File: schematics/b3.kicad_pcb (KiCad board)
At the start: 2 copper layers, 69.5 x 25 mm, 40 parts, among them J1 PowerInput, J2 PowerPassThru, J3 OutputPins, U1 INA128, U2 INA128, U3 INA128, U4 INA128

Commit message: polished b3 some more
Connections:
- J3 pad 2: /out3 -> /out2
- J3 pad 3: /out4 -> /out3
- J3 pad 4: /out2 -> /out4
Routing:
- net /out3: track 27.0 -> 31.2 mm
- net /out2: track 25.4 -> 28.0 mm, vias 0 -> 1
- net VCC: vias 7 -> 6
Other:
- board text added: "GND V+ Vref"
- board text added: "gain"
- board text added: "out1"
- board text added: "out4"

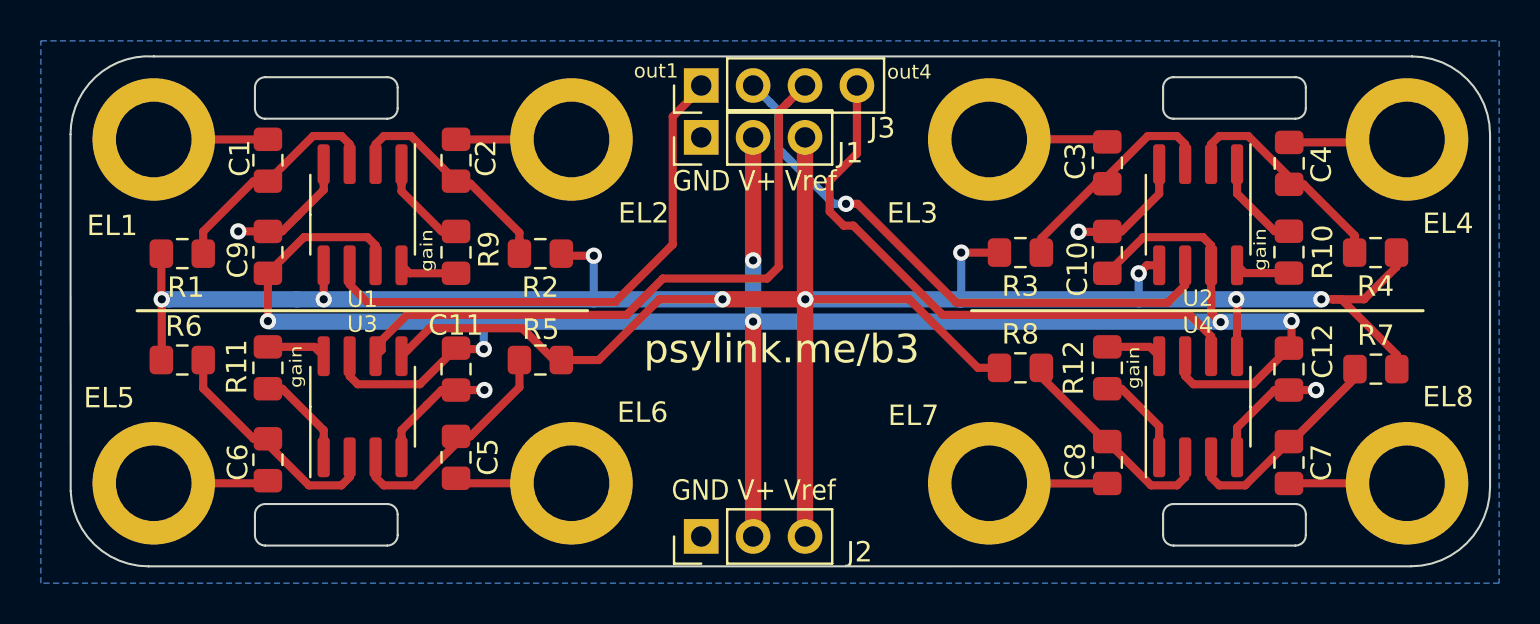
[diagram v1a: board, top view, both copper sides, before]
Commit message: enlarge rubber band holes
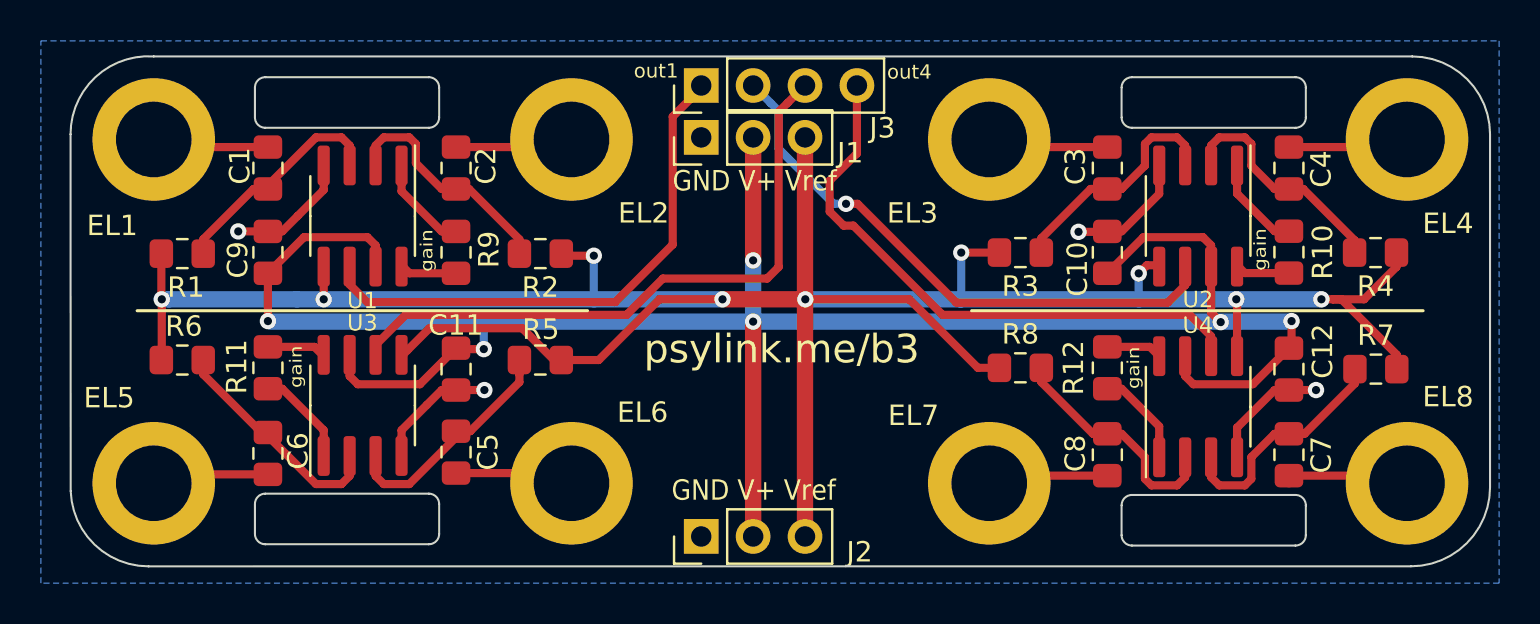
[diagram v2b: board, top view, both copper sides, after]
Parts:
- moved C1 0.38 mm to (35.1, 30.9)
- moved C2 0.38 mm to (44.3, 30.9)
- moved C7 0.38 mm to (85.0, 44.9)
- moved C8 0.38 mm to (76.1, 44.9)
- moved C6 0.31 mm to (35.1, 44.8), turned to 90 degrees
- moved C5 0.25 mm to (44.3, 44.8)
- moved C3 0.25 mm to (76.1, 30.9)
- moved C4 0.23 mm to (85.0, 30.9)
- moved U1 0.06 mm to (39.7, 33.2)
- moved U2 0.06 mm to (80.6, 33.2)
- moved U3 0.06 mm to (39.7, 42.5)
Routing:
- net Net-(C8-Pad1): track 11.1 -> 11.6 mm
- net Net-(C7-Pad2): track 11.1 -> 11.6 mm
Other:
- outline, holes or cut-outs redrawn

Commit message: final polishing of b3 before ordering
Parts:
- turned C6 to 270 degrees

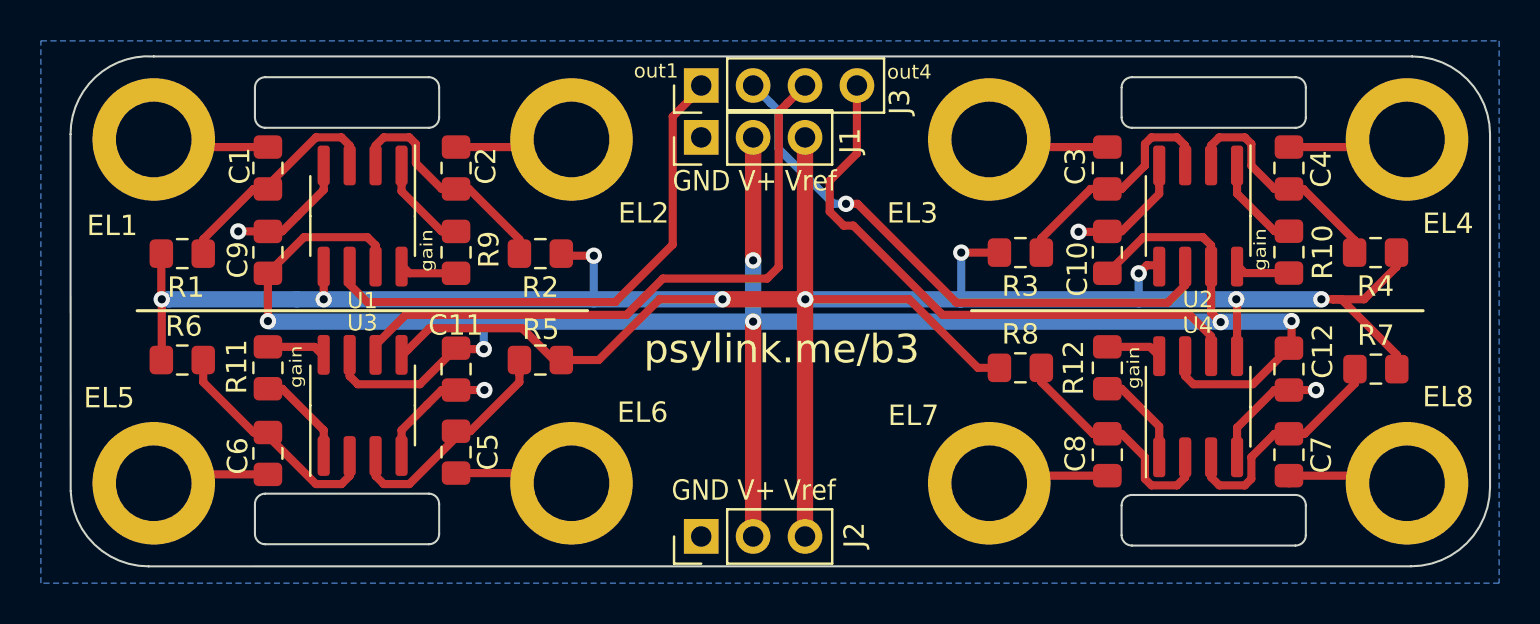
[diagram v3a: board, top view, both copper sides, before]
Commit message: last minute change adding electrode test pins to b3
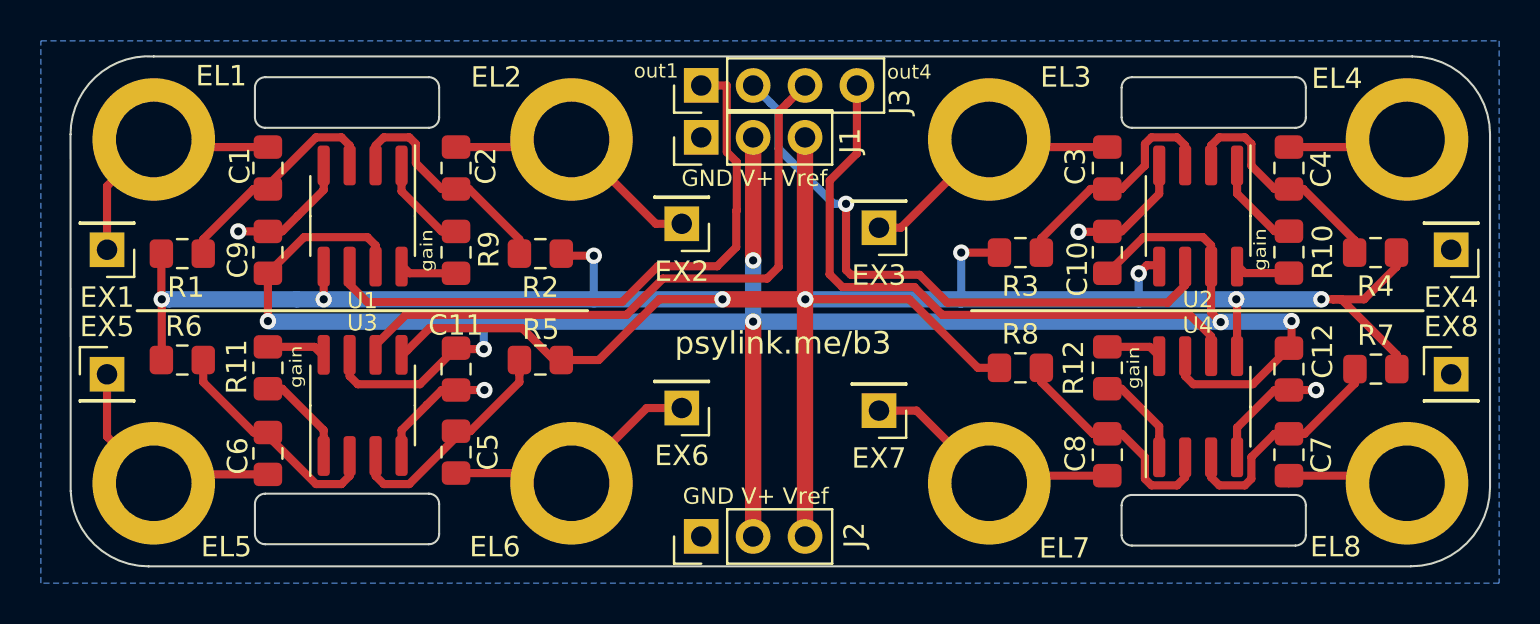
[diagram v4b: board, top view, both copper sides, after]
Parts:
- added EX1: Conn_01x01, Connector_PinHeader_2.54mm:PinHeader_1x01_P2.54mm_Vertical, F.Cu at (27.2, 34.9)
- added EX2: Conn_01x01, Connector_PinHeader_2.54mm:PinHeader_1x01_P2.54mm_Vertical, F.Cu at (55.3, 33.6)
- added EX3: Conn_01x01, Connector_PinHeader_2.54mm:PinHeader_1x01_P2.54mm_Vertical, F.Cu at (65.0, 33.8)
- added EX4: Conn_01x01, Connector_PinHeader_2.54mm:PinHeader_1x01_P2.54mm_Vertical, F.Cu at (93.0, 34.9)
- added EX5: Conn_01x01, Connector_PinHeader_2.54mm:PinHeader_1x01_P2.54mm_Vertical, F.Cu at (27.2, 41.0)
- added EX6: Conn_01x01, Connector_PinHeader_2.54mm:PinHeader_1x01_P2.54mm_Vertical, F.Cu at (55.3, 42.6)
- added EX7: Conn_01x01, Connector_PinHeader_2.54mm:PinHeader_1x01_P2.54mm_Vertical, F.Cu at (65.0, 42.7)
- added EX8: Conn_01x01, Connector_PinHeader_2.54mm:PinHeader_1x01_P2.54mm_Vertical, F.Cu at (93.0, 41.0)
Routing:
- net /in3: track 5.93 -> 13.1 mm
- net /in2: track 5.81 -> 12.9 mm
- net /in6: track 5.86 -> 12.8 mm
- net /in7: track 5.93 -> 12.8 mm
- net /in1: track 5.74 -> 12.2 mm
- net /in5: track 5.77 -> 12.0 mm
- net /out1: track 26.8 -> 30.8 mm
- net /out2: track 28.0 -> 29.9 mm
- net /out4: track 28.9 -> 30.7 mm

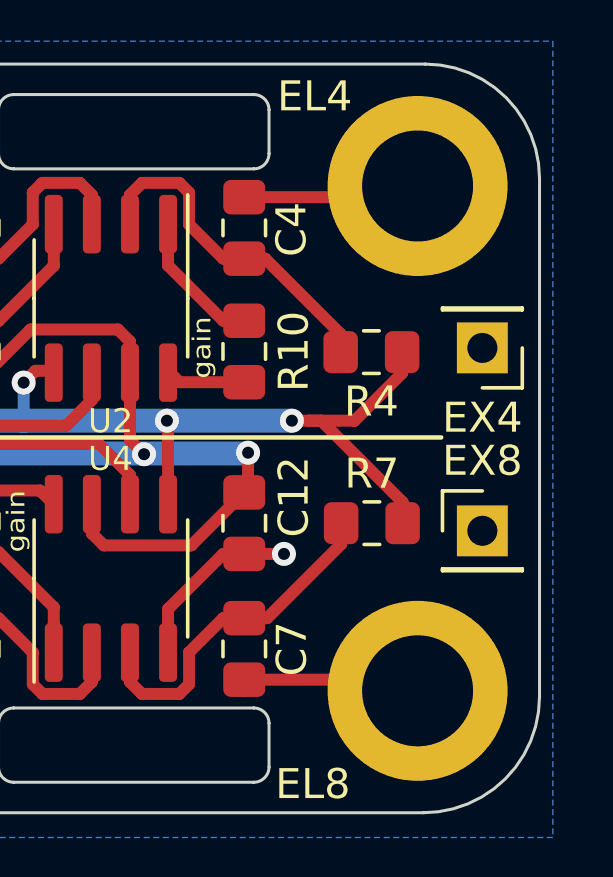
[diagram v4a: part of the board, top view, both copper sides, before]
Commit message: fix missing connections at EX4 and EX8
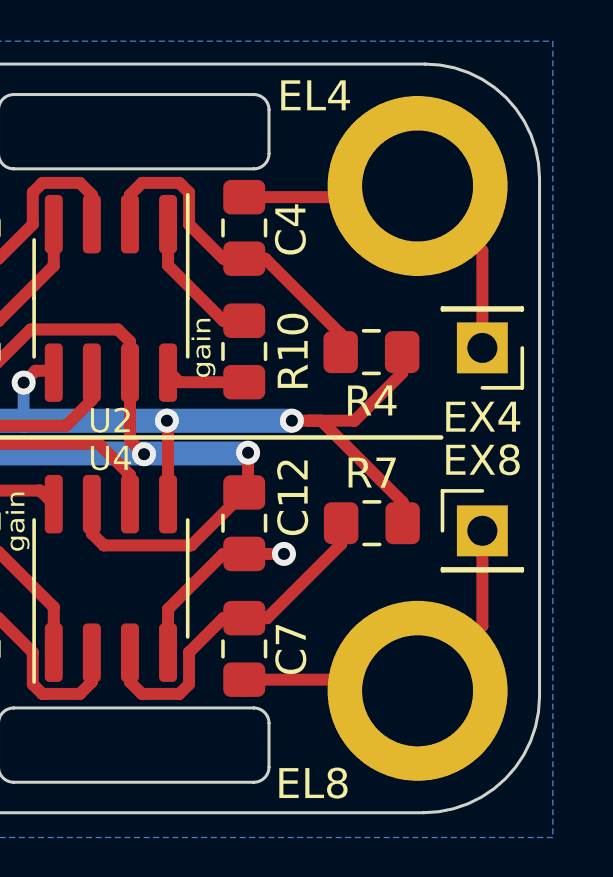
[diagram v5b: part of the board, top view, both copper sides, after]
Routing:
- net /in4: track 5.93 -> 12.2 mm
- net /in8: track 5.95 -> 12.2 mm
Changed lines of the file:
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@@
     (thickness 1.6)
     (drawings 56)
-    (tracks 302)
+    (tracks 306)
     (zones 0)
     (modules 48)
@@
   (segment (start 90.433 29.836) (end 90.805 29.464) (width 0.4) (layer F.Cu) (net 8))
   (segment (start 85.0265 29.836) (end 90.433 29.836) (width 0.4) (layer F.Cu) (net 8))
+  (segment (start 92.964 31.623) (end 90.805 29.464) (width 0.4) (layer F.Cu) (net 8))
+  (segment (start 92.964 34.8615) (end 92.964 31.623) (width 0.4) (layer F.Cu) (net 8))
   (segment (start 47.362 40.959) (end 47.362 40.259) (width 0.4) (layer F.Cu) (net 9))
   (segment (start 47.362 41.34) (end 47.362 40.959) (width 0.4) (layer F.Cu) (net 9))
@@
   (segment (start 90.433 45.9195) (end 90.805 46.2915) (width 0.4) (layer F.Cu) (net 16))
   (segment (start 85.0265 45.9195) (end 90.433 45.9195) (width 0.4) (layer F.Cu) (net 16))
+  (segment (start 92.964 44.1325) (end 90.805 46.2915) (width 0.4) (layer F.Cu) (net 16))
+  (segment (start 92.964 40.9575) (end 92.964 44.1325) (width 0.4) (layer F.Cu) (net 16))
   (segment (start 41.5925 44.045) (end 41.5925 45.02) (width 0.4) (layer F.Cu) (net 17))
   (segment (start 43.5595 41.7285) (end 42.8345 42.4535) (width 0.4) (layer F.Cu) (net 17))
